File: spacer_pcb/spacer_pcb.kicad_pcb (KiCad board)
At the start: 2 copper layers, 8.8 x 37.2 mm, 1 part, among them J2 Conn_02x15_Odd_Even

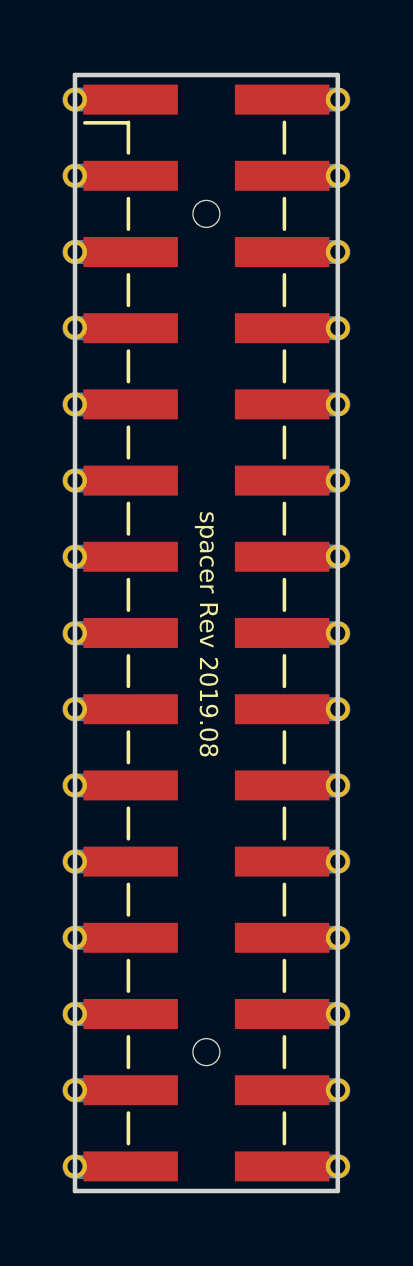
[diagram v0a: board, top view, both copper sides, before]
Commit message: Update spacer pad style
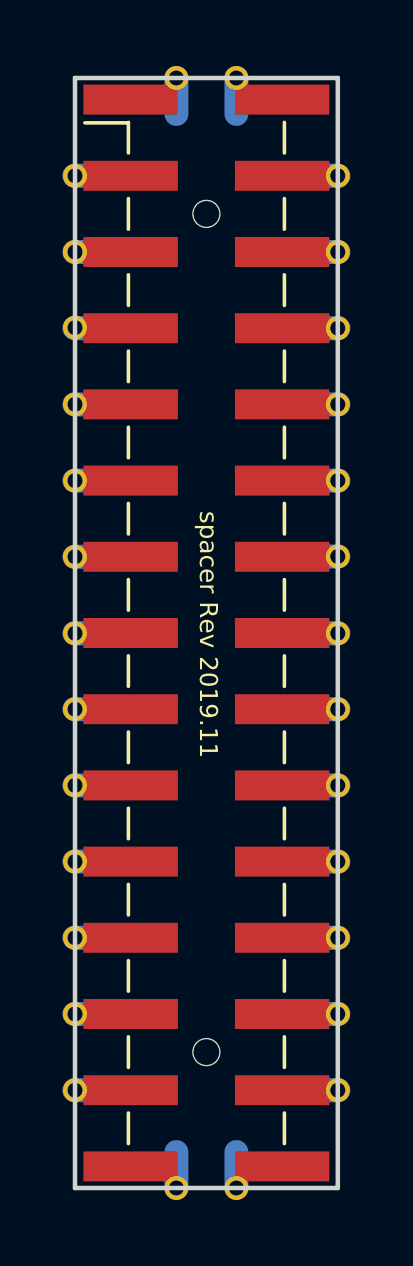
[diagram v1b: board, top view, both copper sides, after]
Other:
- board size 8.8 x 37.2 mm -> 8.8 x 37 mm
- board text added: "spacer Rev 2019.11"
- board text removed: "spacer Rev 2019.08"
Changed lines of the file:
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@@
     (fp_line (start -1.59 -19.05) (end 2.54 -19.05) (layer F.Fab) (width 0.1))
     (fp_line (start 2.54 19.05) (end -2.54 19.05) (layer F.Fab) (width 0.1))
-    (fp_line (start -4.38 18.6) (end 4.38 18.6) (layer Edge.Cuts) (width 0.15))
-    (fp_line (start 4.38 18.6) (end 4.38 -18.6) (layer Edge.Cuts) (width 0.15))
-    (fp_line (start 4.38 -18.6) (end -4.38 -18.6) (layer Edge.Cuts) (width 0.15))
-    (fp_line (start -4.38 -18.6) (end -4.38 18.6) (layer Edge.Cuts) (width 0.15))
+    (fp_line (start -4.38 18.5) (end 4.38 18.5) (layer Edge.Cuts) (width 0.15))
+    (fp_line (start 4.38 18.5) (end 4.38 -18.5) (layer Edge.Cuts) (width 0.15))
+    (fp_line (start 4.38 -18.5) (end -4.38 -18.5) (layer Edge.Cuts) (width 0.15))
+    (fp_line (start -4.38 -18.5) (end -4.38 18.5) (layer Edge.Cuts) (width 0.15))
     (pad "" np_thru_hole circle (at 0 13.97) (size 0.9 0.9) (drill 0.9) (layers *.Cu *.Mask))
     (pad "" np_thru_hole circle (at 0 -13.97) (size 0.9 0.9) (drill 0.9) (layers *.Cu *.Mask))
@@
     (pad 1 smd rect (at -2.525 -17.78) (size 3.15 1) (layers F.Cu F.Paste F.Mask)
       (net 30 "Net-(J2-Pad1)"))
-    (pad 1 smd oval (at -3.3 -17.78) (size 3 0.8) (layers B.Cu B.Paste B.Mask)
+    (pad 1 smd oval (at -1 -17.9 90) (size 2 0.8) (layers B.Cu B.Paste B.Mask)
       (net 30 "Net-(J2-Pad1)"))
     (pad 3 smd oval (at -3.3 -15.24) (size 3 0.8) (layers B.Cu B.Paste B.Mask)
@@
     (pad 27 smd oval (at -3.3 15.24) (size 3 0.8) (layers B.Cu B.Paste B.Mask)
       (net 17 "Net-(J2-Pad27)"))
-    (pad 29 smd oval (at -3.3 17.8) (size 3 0.8) (layers B.Cu B.Paste B.Mask)
+    (pad 29 smd oval (at -1 17.9 90) (size 2 0.8) (layers B.Cu B.Paste B.Mask)
       (net 16 "Net-(J2-Pad29)"))
-    (pad 2 smd oval (at 3.3 -17.78) (size 3 0.8) (layers B.Cu B.Paste B.Mask)
+    (pad 2 smd oval (at 1 -17.9 90) (size 2 0.8) (layers B.Cu B.Paste B.Mask)
       (net 1 "Net-(J2-Pad2)"))
     (pad 4 smd oval (at 3.3 -15.24) (size 3 0.8) (layers B.Cu B.Paste B.Mask)
@@
     (pad 28 smd oval (at 3.3 15.24) (size 3 0.8) (layers B.Cu B.Paste B.Mask)
       (net 14 "Net-(J2-Pad28)"))
-    (pad 30 smd oval (at 3.3 17.78) (size 3 0.8) (layers B.Cu B.Paste B.Mask)
+    (pad 30 smd oval (at 1 17.9 90) (size 2 0.8) (layers B.Cu B.Paste B.Mask)
       (net 15 "Net-(J2-Pad30)"))
-    (pad 1 thru_hole circle (at -4.38 -17.78) (size 0.8 0.8) (drill 0.5) (layers *.Cu *.Mask)
+    (pad 1 thru_hole circle (at -1 -18.5) (size 0.8 0.8) (drill 0.5) (layers *.Cu *.Mask)
       (net 30 "Net-(J2-Pad1)"))
     (pad 3 thru_hole circle (at -4.38 -15.24) (size 0.8 0.8) (drill 0.5) (layers *.Cu *.Mask)
@@
     (pad 27 thru_hole circle (at -4.38 15.24) (size 0.8 0.8) (drill 0.5) (layers *.Cu *.Mask)
       (net 17 "Net-(J2-Pad27)"))
-    (pad 29 thru_hole circle (at -4.38 17.78) (size 0.8 0.8) (drill 0.5) (layers *.Cu *.Mask)
+    (pad 29 thru_hole circle (at -1 18.5) (size 0.8 0.8) (drill 0.5) (layers *.Cu *.Mask)
       (net 16 "Net-(J2-Pad29)"))
-    (pad 2 thru_hole circle (at 4.38 -17.78) (size 0.8 0.8) (drill 0.5) (layers *.Cu *.Mask)
+    (pad 2 thru_hole circle (at 1 -18.5) (size 0.8 0.8) (drill 0.5) (layers *.Cu *.Mask)
       (net 1 "Net-(J2-Pad2)"))
     (pad 4 thru_hole circle (at 4.38 -15.24) (size 0.8 0.8) (drill 0.5) (layers *.Cu *.Mask)
@@
     (pad 28 thru_hole circle (at 4.38 15.24) (size 0.8 0.8) (drill 0.5) (layers *.Cu *.Mask)
       (net 14 "Net-(J2-Pad28)"))
-    (pad 30 thru_hole circle (at 4.38 17.78) (size 0.8 0.8) (drill 0.5) (layers *.Cu *.Mask)
+    (pad 30 thru_hole circle (at 1 18.5) (size 0.8 0.8) (drill 0.5) (layers *.Cu *.Mask)
       (net 15 "Net-(J2-Pad30)"))
     (model ${KISYS3DMOD}/Connector_PinHeader_2.54mm.3dshapes/PinHeader_2x15_P2.54mm_Vertical_SMD.wrl
@@
     )
   )
-  (gr_text "spacer Rev 2019.08" (at 122.0089 78.2828 270) (layer F.SilkS)
+  (gr_text "spacer Rev 2019.11" (at 122.0089 78.2828 270) (layer F.SilkS)
     (effects (font (size 0.6 0.6) (thickness 0.15)))
   )

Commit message: Change hole size on spacer pcb larger
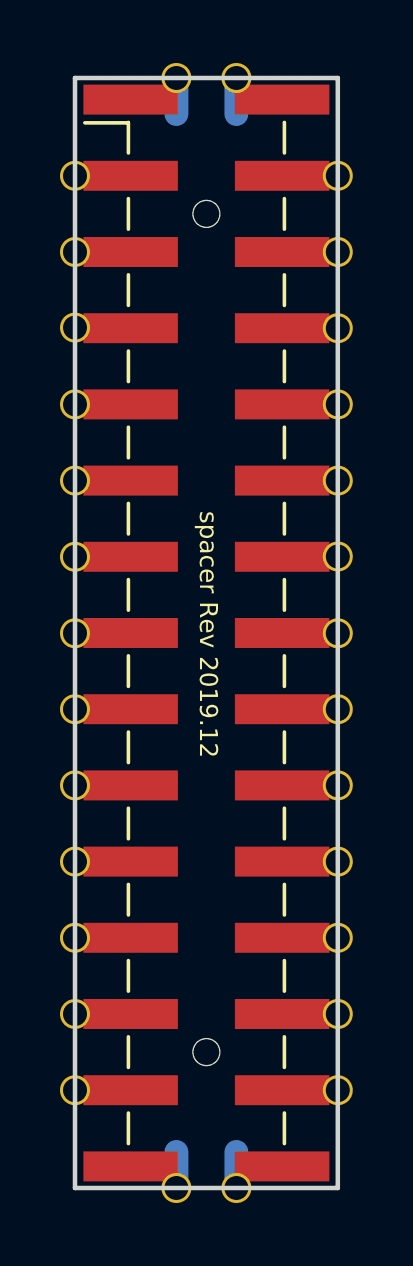
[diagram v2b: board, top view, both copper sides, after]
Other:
- board text added: "spacer Rev 2019.12"
- board text removed: "spacer Rev 2019.11"
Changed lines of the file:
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@@
-(kicad_pcb (version 20171130) (host pcbnew 5.1.4-e60b266~84~ubuntu18.04.1)
+(kicad_pcb (version 20171130) (host pcbnew 5.1.5-52549c5~84~ubuntu18.04.1)
   (general
     (thickness 1.6)
@@
     (pad 30 smd oval (at 1 17.9 90) (size 2 0.8) (layers B.Cu B.Paste B.Mask)
       (net 15 "Net-(J2-Pad30)"))
-    (pad 1 thru_hole circle (at -1 -18.5) (size 0.8 0.8) (drill 0.5) (layers *.Cu *.Mask)
+    (pad 1 thru_hole circle (at -1 -18.5) (size 1 1) (drill 0.8) (layers *.Cu *.Mask)
       (net 30 "Net-(J2-Pad1)"))
-    (pad 3 thru_hole circle (at -4.38 -15.24) (size 0.8 0.8) (drill 0.5) (layers *.Cu *.Mask)
+    (pad 3 thru_hole circle (at -4.38 -15.24) (size 1 1) (drill 0.8) (layers *.Cu *.Mask)
       (net 29 "Net-(J2-Pad3)"))
-    (pad 5 thru_hole circle (at -4.38 -12.7) (size 0.8 0.8) (drill 0.5) (layers *.Cu *.Mask)
+    (pad 5 thru_hole circle (at -4.38 -12.7) (size 1 1) (drill 0.8) (layers *.Cu *.Mask)
       (net 28 "Net-(J2-Pad5)"))
-    (pad 7 thru_hole circle (at -4.38 -10.18) (size 0.8 0.8) (drill 0.5) (layers *.Cu *.Mask)
+    (pad 7 thru_hole circle (at -4.38 -10.18) (size 1 1) (drill 0.8) (layers *.Cu *.Mask)
       (net 27 "Net-(J2-Pad7)"))
-    (pad 9 thru_hole circle (at -4.38 -7.62) (size 0.8 0.8) (drill 0.5) (layers *.Cu *.Mask)
+    (pad 9 thru_hole circle (at -4.38 -7.62) (size 1 1) (drill 0.8) (layers *.Cu *.Mask)
       (net 26 "Net-(J2-Pad9)"))
-    (pad 11 thru_hole circle (at -4.38 -5.08) (size 0.8 0.8) (drill 0.5) (layers *.Cu *.Mask)
+    (pad 11 thru_hole circle (at -4.38 -5.08) (size 1 1) (drill 0.8) (layers *.Cu *.Mask)
       (net 25 "Net-(J2-Pad11)"))
-    (pad 13 thru_hole circle (at -4.38 -2.54) (size 0.8 0.8) (drill 0.5) (layers *.Cu *.Mask)
+    (pad 13 thru_hole circle (at -4.38 -2.54) (size 1 1) (drill 0.8) (layers *.Cu *.Mask)
       (net 24 "Net-(J2-Pad13)"))
-    (pad 15 thru_hole circle (at -4.38 0.01) (size 0.8 0.8) (drill 0.5) (layers *.Cu *.Mask)
+    (pad 15 thru_hole circle (at -4.38 0.01) (size 1 1) (drill 0.8) (layers *.Cu *.Mask)
       (net 23 "Net-(J2-Pad15)"))
-    (pad 17 thru_hole circle (at -4.38 2.54) (size 0.8 0.8) (drill 0.5) (layers *.Cu *.Mask)
+    (pad 17 thru_hole circle (at -4.38 2.54) (size 1 1) (drill 0.8) (layers *.Cu *.Mask)
       (net 22 "Net-(J2-Pad17)"))
-    (pad 19 thru_hole circle (at -4.38 5.08) (size 0.8 0.8) (drill 0.5) (layers *.Cu *.Mask)
+    (pad 19 thru_hole circle (at -4.38 5.08) (size 1 1) (drill 0.8) (layers *.Cu *.Mask)
       (net 21 "Net-(J2-Pad19)"))
-    (pad 21 thru_hole circle (at -4.38 7.62) (size 0.8 0.8) (drill 0.5) (layers *.Cu *.Mask)
+    (pad 21 thru_hole circle (at -4.38 7.62) (size 1 1) (drill 0.8) (layers *.Cu *.Mask)
       (net 20 "Net-(J2-Pad21)"))
-    (pad 23 thru_hole circle (at -4.38 10.16) (size 0.8 0.8) (drill 0.5) (layers *.Cu *.Mask)
+    (pad 23 thru_hole circle (at -4.38 10.16) (size 1 1) (drill 0.8) (layers *.Cu *.Mask)
       (net 19 "Net-(J2-Pad23)"))
-    (pad 25 thru_hole circle (at -4.38 12.7) (size 0.8 0.8) (drill 0.5) (layers *.Cu *.Mask)
+    (pad 25 thru_hole circle (at -4.38 12.7) (size 1 1) (drill 0.8) (layers *.Cu *.Mask)
       (net 18 "Net-(J2-Pad25)"))
-    (pad 27 thru_hole circle (at -4.38 15.24) (size 0.8 0.8) (drill 0.5) (layers *.Cu *.Mask)
+    (pad 27 thru_hole circle (at -4.38 15.24) (size 1 1) (drill 0.8) (layers *.Cu *.Mask)
       (net 17 "Net-(J2-Pad27)"))
-    (pad 29 thru_hole circle (at -1 18.5) (size 0.8 0.8) (drill 0.5) (layers *.Cu *.Mask)
+    (pad 29 thru_hole circle (at -1 18.5) (size 1 1) (drill 0.8) (layers *.Cu *.Mask)
       (net 16 "Net-(J2-Pad29)"))
-    (pad 2 thru_hole circle (at 1 -18.5) (size 0.8 0.8) (drill 0.5) (layers *.Cu *.Mask)
+    (pad 2 thru_hole circle (at 1 -18.5) (size 1 1) (drill 0.8) (layers *.Cu *.Mask)
       (net 1 "Net-(J2-Pad2)"))
-    (pad 4 thru_hole circle (at 4.38 -15.24) (size 0.8 0.8) (drill 0.5) (layers *.Cu *.Mask)
+    (pad 4 thru_hole circle (at 4.38 -15.24) (size 1 1) (drill 0.8) (layers *.Cu *.Mask)
       (net 2 "Net-(J2-Pad4)"))
-    (pad 6 thru_hole circle (at 4.38 -12.7) (size 0.8 0.8) (drill 0.5) (layers *.Cu *.Mask)
+    (pad 6 thru_hole circle (at 4.38 -12.7) (size 1 1) (drill 0.8) (layers *.Cu *.Mask)
       (net 3 "Net-(J2-Pad6)"))
-    (pad 8 thru_hole circle (at 4.38 -10.16) (size 0.8 0.8) (drill 0.5) (layers *.Cu *.Mask)
+    (pad 8 thru_hole circle (at 4.38 -10.16) (size 1 1) (drill 0.8) (layers *.Cu *.Mask)
       (net 4 "Net-(J2-Pad8)"))
-    (pad 10 thru_hole circle (at 4.38 -7.62) (size 0.8 0.8) (drill 0.5) (layers *.Cu *.Mask)
+    (pad 10 thru_hole circle (at 4.38 -7.62) (size 1 1) (drill 0.8) (layers *.Cu *.Mask)
       (net 5 "Net-(J2-Pad10)"))
-    (pad 12 thru_hole circle (at 4.38 -5.08) (size 0.8 0.8) (drill 0.5) (layers *.Cu *.Mask)
+    (pad 12 thru_hole circle (at 4.38 -5.08) (size 1 1) (drill 0.8) (layers *.Cu *.Mask)
       (net 6 "Net-(J2-Pad12)"))
-    (pad 14 thru_hole circle (at 4.38 -2.55) (size 0.8 0.8) (drill 0.5) (layers *.Cu *.Mask)
+    (pad 14 thru_hole circle (at 4.38 -2.55) (size 1 1) (drill 0.8) (layers *.Cu *.Mask)
       (net 7 "Net-(J2-Pad14)"))
-    (pad 16 thru_hole circle (at 4.38 0.01) (size 0.8 0.8) (drill 0.5) (layers *.Cu *.Mask)
+    (pad 16 thru_hole circle (at 4.38 0.01) (size 1 1) (drill 0.8) (layers *.Cu *.Mask)
       (net 8 "Net-(J2-Pad16)"))
-    (pad 18 thru_hole circle (at 4.38 2.54) (size 0.8 0.8) (drill 0.5) (layers *.Cu *.Mask)
+    (pad 18 thru_hole circle (at 4.38 2.54) (size 1 1) (drill 0.8) (layers *.Cu *.Mask)
       (net 9 "Net-(J2-Pad18)"))
-    (pad 20 thru_hole circle (at 4.38 5.08) (size 0.8 0.8) (drill 0.5) (layers *.Cu *.Mask)
+    (pad 20 thru_hole circle (at 4.38 5.08) (size 1 1) (drill 0.8) (layers *.Cu *.Mask)
       (net 10 "Net-(J2-Pad20)"))
-    (pad 22 thru_hole circle (at 4.38 7.62) (size 0.8 0.8) (drill 0.5) (layers *.Cu *.Mask)
+    (pad 22 thru_hole circle (at 4.38 7.62) (size 1 1) (drill 0.8) (layers *.Cu *.Mask)
       (net 11 "Net-(J2-Pad22)"))
-    (pad 24 thru_hole circle (at 4.38 10.16) (size 0.8 0.8) (drill 0.5) (layers *.Cu *.Mask)
+    (pad 24 thru_hole circle (at 4.38 10.16) (size 1 1) (drill 0.8) (layers *.Cu *.Mask)
       (net 12 "Net-(J2-Pad24)"))
-    (pad 26 thru_hole circle (at 4.38 12.7) (size 0.8 0.8) (drill 0.5) (layers *.Cu *.Mask)
+    (pad 26 thru_hole circle (at 4.38 12.7) (size 1 1) (drill 0.8) (layers *.Cu *.Mask)
       (net 13 "Net-(J2-Pad26)"))
-    (pad 28 thru_hole circle (at 4.38 15.24) (size 0.8 0.8) (drill 0.5) (layers *.Cu *.Mask)
+    (pad 28 thru_hole circle (at 4.38 15.24) (size 1 1) (drill 0.8) (layers *.Cu *.Mask)
       (net 14 "Net-(J2-Pad28)"))
-    (pad 30 thru_hole circle (at 1 18.5) (size 0.8 0.8) (drill 0.5) (layers *.Cu *.Mask)
+    (pad 30 thru_hole circle (at 1 18.5) (size 1 1) (drill 0.8) (layers *.Cu *.Mask)
       (net 15 "Net-(J2-Pad30)"))
     (model ${KISYS3DMOD}/Connector_PinHeader_2.54mm.3dshapes/PinHeader_2x15_P2.54mm_Vertical_SMD.wrl
@@
     )
   )
-  (gr_text "spacer Rev 2019.11" (at 122.0089 78.2828 270) (layer F.SilkS)
+  (gr_text "spacer Rev 2019.12" (at 122.0089 78.2828 270) (layer F.SilkS)
     (effects (font (size 0.6 0.6) (thickness 0.15)))
   )

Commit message: Update size of pads
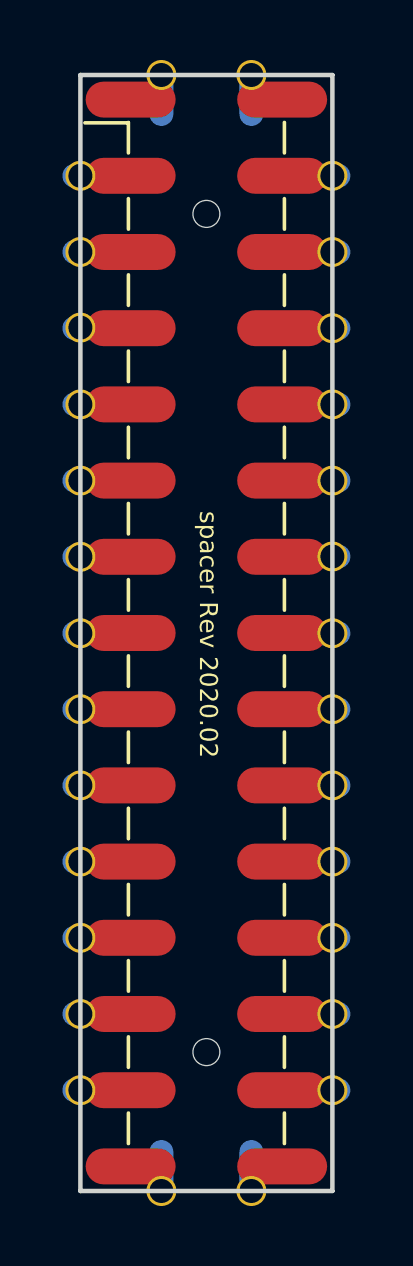
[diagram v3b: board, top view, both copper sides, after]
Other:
- board size 8.8 x 37 mm -> 8.4 x 37.2 mm
- board text added: "spacer Rev 2020.02"
- board text removed: "spacer Rev 2019.12"

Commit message: Add holes for socket to spacer pcb
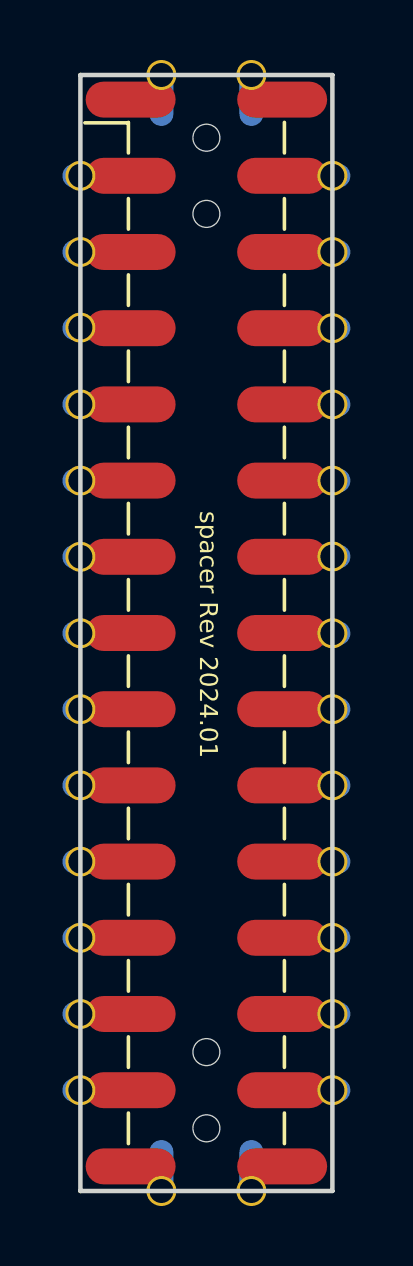
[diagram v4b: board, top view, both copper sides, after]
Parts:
- J2: footprint footprints:PinHeader_2x15_P2.54mm_M5Stack_SpacerPCB -> footprints:PinHeader_2x15_P2.54mm_M5Stack_SpacerPCB_with_holes_for_socket
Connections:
- J2 pad 1: Net-(J2-Pad1) -> unconnected-(J2-Pin_1-Pad1)
- J2 pad 10: Net-(J2-Pad10) -> unconnected-(J2-Pin_10-Pad10)
- J2 pad 11: Net-(J2-Pad11) -> unconnected-(J2-Pin_11-Pad11)
- J2 pad 12: Net-(J2-Pad12) -> unconnected-(J2-Pin_12-Pad12)
- J2 pad 13: Net-(J2-Pad13) -> unconnected-(J2-Pin_13-Pad13)
- J2 pad 14: Net-(J2-Pad14) -> unconnected-(J2-Pin_14-Pad14)
- J2 pad 15: Net-(J2-Pad15) -> unconnected-(J2-Pin_15-Pad15)
- J2 pad 16: Net-(J2-Pad16) -> unconnected-(J2-Pin_16-Pad16)
- J2 pad 17: Net-(J2-Pad17) -> unconnected-(J2-Pin_17-Pad17)
- J2 pad 18: Net-(J2-Pad18) -> unconnected-(J2-Pin_18-Pad18)
- J2 pad 19: Net-(J2-Pad19) -> unconnected-(J2-Pin_19-Pad19)
- J2 pad 2: Net-(J2-Pad2) -> unconnected-(J2-Pin_2-Pad2)
- J2 pad 20: Net-(J2-Pad20) -> unconnected-(J2-Pin_20-Pad20)
- J2 pad 21: Net-(J2-Pad21) -> unconnected-(J2-Pin_21-Pad21)
- J2 pad 22: Net-(J2-Pad22) -> unconnected-(J2-Pin_22-Pad22)
- J2 pad 23: Net-(J2-Pad23) -> unconnected-(J2-Pin_23-Pad23)
- J2 pad 24: Net-(J2-Pad24) -> unconnected-(J2-Pin_24-Pad24)
- J2 pad 25: Net-(J2-Pad25) -> unconnected-(J2-Pin_25-Pad25)
- J2 pad 26: Net-(J2-Pad26) -> unconnected-(J2-Pin_26-Pad26)
- J2 pad 27: Net-(J2-Pad27) -> unconnected-(J2-Pin_27-Pad27)
- J2 pad 28: Net-(J2-Pad28) -> unconnected-(J2-Pin_28-Pad28)
- J2 pad 29: Net-(J2-Pad29) -> unconnected-(J2-Pin_29-Pad29)
- J2 pad 3: Net-(J2-Pad3) -> unconnected-(J2-Pin_3-Pad3)
- J2 pad 30: Net-(J2-Pad30) -> unconnected-(J2-Pin_30-Pad30)
- J2 pad 4: Net-(J2-Pad4) -> unconnected-(J2-Pin_4-Pad4)
- J2 pad 5: Net-(J2-Pad5) -> unconnected-(J2-Pin_5-Pad5)
- J2 pad 6: Net-(J2-Pad6) -> unconnected-(J2-Pin_6-Pad6)
- J2 pad 7: Net-(J2-Pad7) -> unconnected-(J2-Pin_7-Pad7)
- J2 pad 8: Net-(J2-Pad8) -> unconnected-(J2-Pin_8-Pad8)
- J2 pad 9: Net-(J2-Pad9) -> unconnected-(J2-Pin_9-Pad9)
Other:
- net class Default removed
- board text added: "spacer Rev 2024.01"
- board text removed: "spacer Rev 2020.02"

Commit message: Expand hole size to 1.0 from 0.9mm
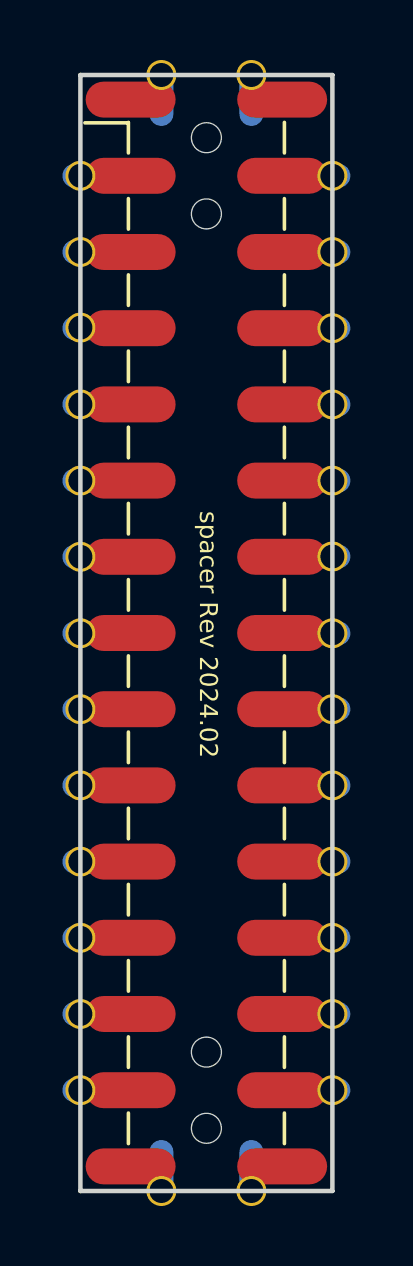
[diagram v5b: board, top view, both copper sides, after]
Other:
- board text added: "spacer Rev 2024.02"
- board text removed: "spacer Rev 2024.01"
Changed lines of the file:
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@@
     (fp_line (start 3.6 18.1) (end 2.54 18.1)
       (stroke (width 0.1) (type solid)) (layer "F.Fab"))
-    (pad "" np_thru_hole circle (at 0 -16.51) (size 0.9 0.9) (drill 0.9) (layers "F&B.Cu" "*.Mask"))
-    (pad "" np_thru_hole circle (at 0 -13.97) (size 0.9 0.9) (drill 0.9) (layers "*.Cu" "*.Mask"))
-    (pad "" np_thru_hole circle (at 0 13.97) (size 0.9 0.9) (drill 0.9) (layers "*.Cu" "*.Mask"))
-    (pad "" np_thru_hole circle (at 0 16.51) (size 0.9 0.9) (drill 0.9) (layers "F&B.Cu" "*.Mask"))
+    (pad "" np_thru_hole circle (at 0 -16.51) (size 0.9 0.9) (drill 1) (layers "F&B.Cu" "*.Mask"))
+    (pad "" np_thru_hole circle (at 0 -13.97) (size 0.9 0.9) (drill 1) (layers "F&B.Cu" "*.Mask"))
+    (pad "" np_thru_hole circle (at 0 13.97) (size 0.9 0.9) (drill 1) (layers "F&B.Cu" "*.Mask"))
+    (pad "" np_thru_hole circle (at 0 16.51) (size 0.9 0.9) (drill 1) (layers "F&B.Cu" "*.Mask"))
     (pad "1" smd oval (at -2.525 -17.78) (size 3 1.2) (layers "F.Cu" "F.Paste" "F.Mask")
       (net 1 "unconnected-(J2-Pin_1-Pad1)") (pinfunction "Pin_1") (pintype "passive+no_connect"))
@@
     )
   )
-  (gr_text "spacer Rev 2024.01" (at 122.0089 78.2828 270) (layer "F.SilkS")
+  (gr_text "spacer Rev 2024.02" (at 122.0089 78.2828 270) (layer "F.SilkS")
     (effects (font (size 0.6 0.6) (thickness 0.15)))
   )
